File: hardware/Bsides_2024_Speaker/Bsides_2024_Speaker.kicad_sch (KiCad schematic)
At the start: 39 parts, among them J1 Conn_02x03_Odd_Even, J2 Battery, J3 Battery, J4 OLED, P1 USB_C_Plug_USB2.0, Q1 DMG3415U-7, SW1 ON, SW2 RESET, SW3 BOOT, SW4 RESET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

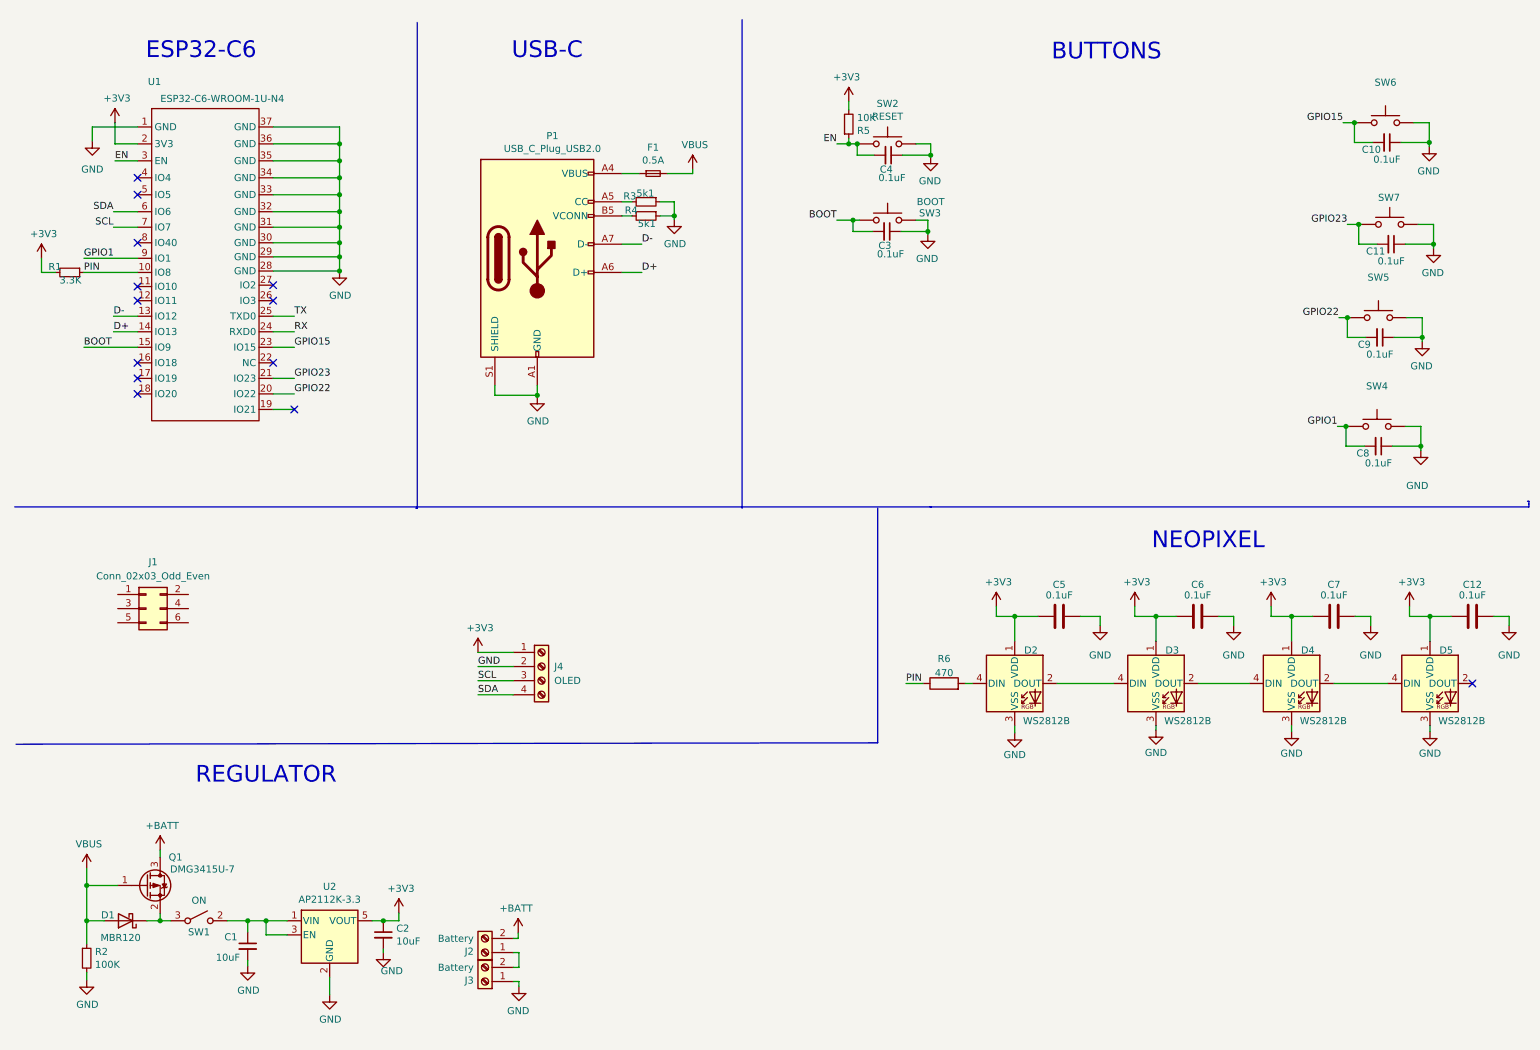
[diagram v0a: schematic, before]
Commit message: feat(Hw):Added_speaker_Badge_Floorplan
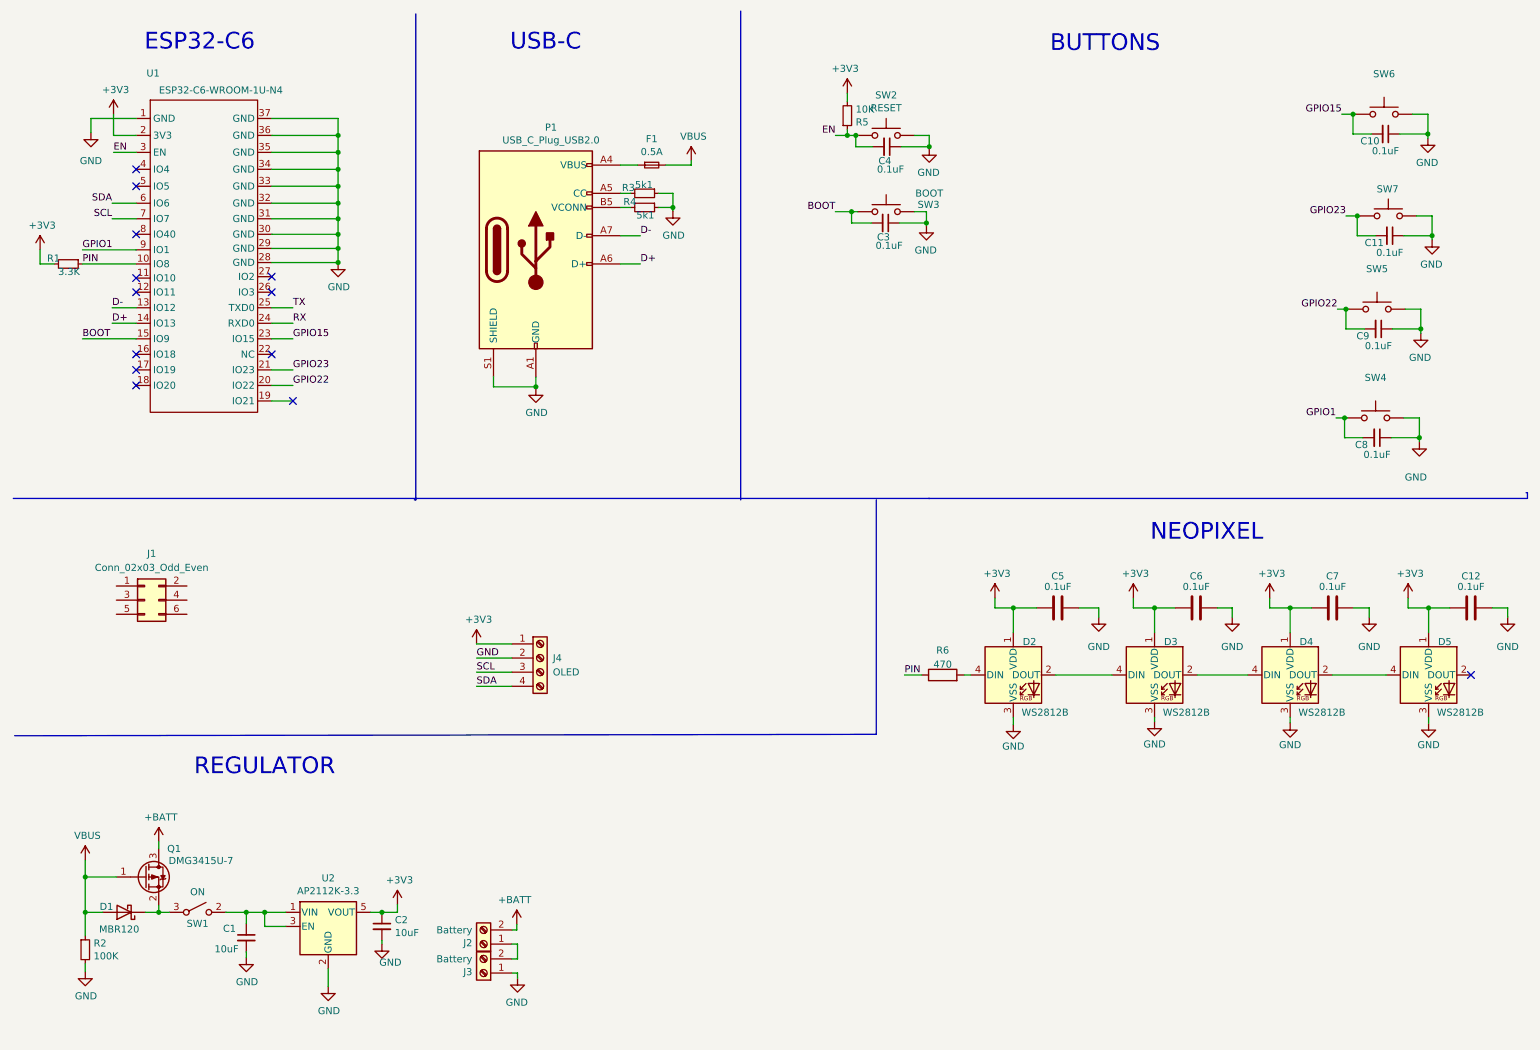
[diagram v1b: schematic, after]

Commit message: feat(Hw):Update_Route_Speaker
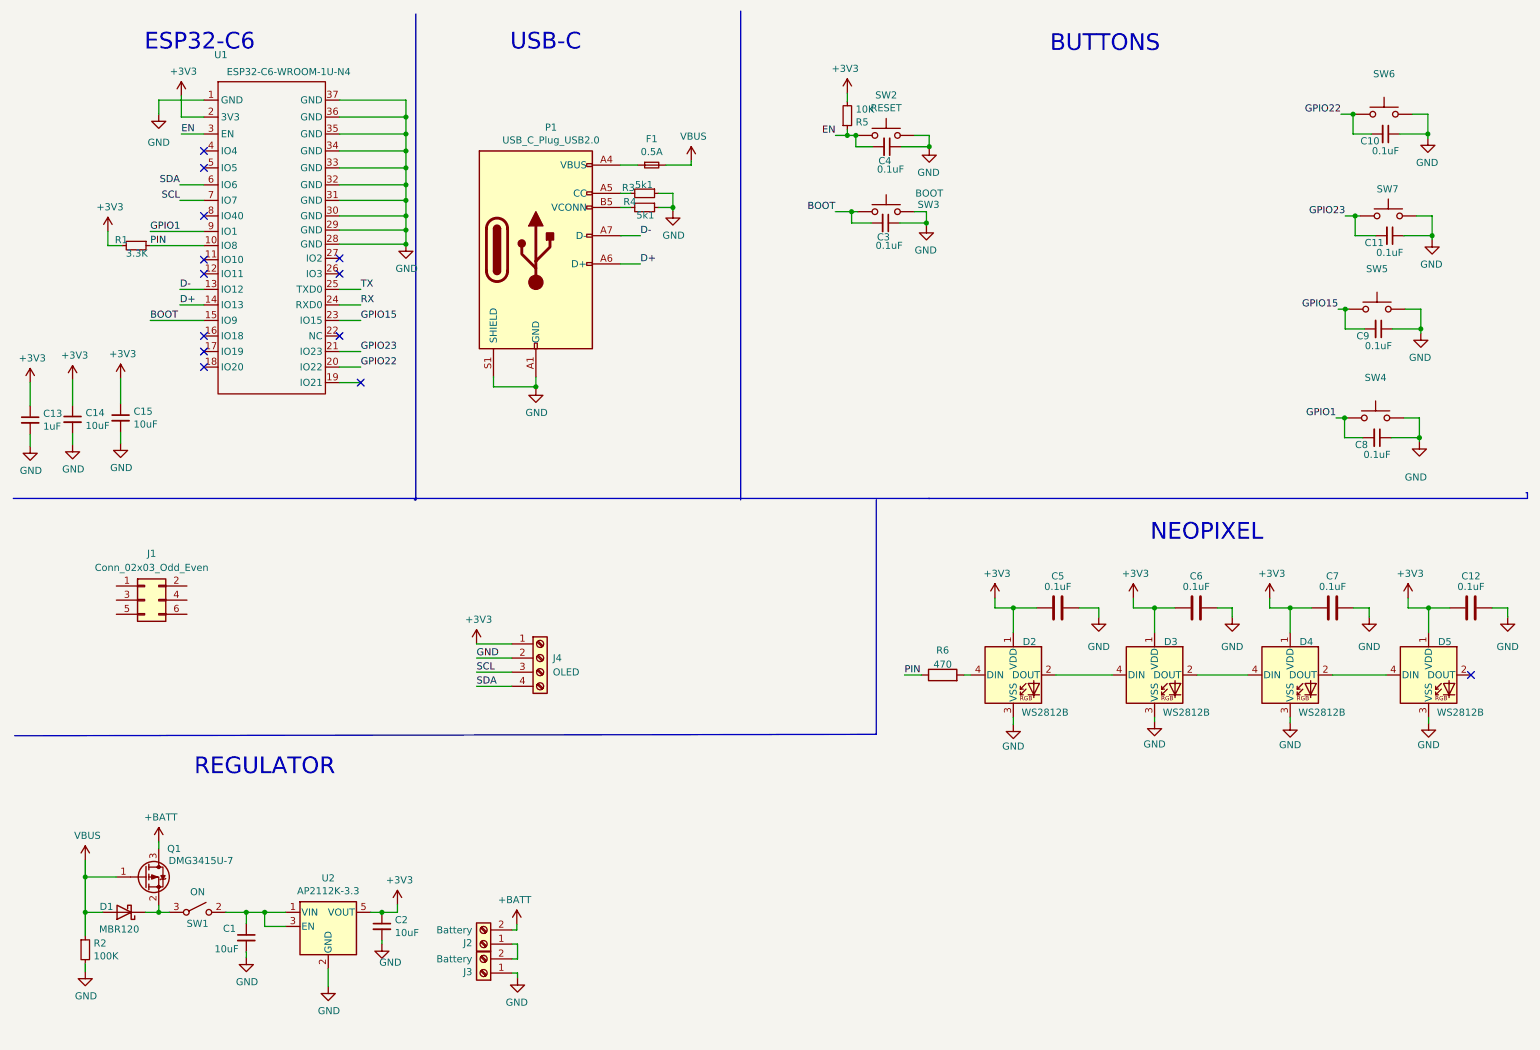
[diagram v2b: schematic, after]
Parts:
- added C13: 1uF, Capacitor_SMD:C_0603_1608Metric, symbol Device:C_Small
- added C14, C15: 10uF, Capacitor_SMD:C_0603_1608Metric, symbol Device:C_Small
- J2, J3: footprint bsides:BH-AAA-A1aj001 -> bsides:BH-AA-A1AJ020
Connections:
- net +3V3: now also C13.1, C14.1, C15.1
- net GND: now also C13.2, C14.2, C15.2
- net GPIO15: now also C9.2, SW5.2; no longer C10.2, SW6.2
- net GPIO22: now also C10.2, SW6.2; no longer C9.2, SW5.2
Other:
- moved on the sheet: R1, U1

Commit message: feat(Hw):Update_PCB_Speaker
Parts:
- J1: value Conn_02x03_Odd_Even -> Add_On
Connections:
- net +3V3: now also J1.1 (Pin_1)
- net GND: now also J1.2 (Pin_2)
- net GPIO1: now also U1.26 (IO3); no longer U1.9 (IO1)
- net SCL: now also J1.4 (Pin_4)
- net SDA: now also J1.3 (Pin_3)
- no-connect marks 13 -> 14
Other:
- moved on the sheet: J2, J3

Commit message: feat:(Hw)Update_PCB_Speaker_Sponsor_Staff
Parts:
- C1, C14, C15, C2: Proveedor (none) -> Mouser; manf# (none) -> GRM188R61E106KA73J
- C10, C11, C8, C9: LCSC# (none) -> C478888; Proveedor (none) -> Mouser; manf# (none) -> KAM15AR71C104KM
- C12, C5, C6, C7: LCSC# C42998 -> C478888; Proveedor LCSC -> Mouser; manf# 0603F104M500NT -> KAM15AR71C104KM
- C13: Proveedor (none) -> Mouser; manf# (none) -> TMK107BJ105KA8T
- C3, C4: Proveedor (none) -> Mouser; manf# (none) -> KAM15AR71C104KM
- D1: Proveedor (none) -> Mouser; manf# MBR120LSF -> MBR120LSFT1G
- D2, D3, D4, D5: manf# WS2812B-Mini -> (none)
- F1: LCSC# - -> (none); Proveedor (none) -> Mouser; manf# MFU0805FF00500P100 -> MFU0805FF00750P100
- P1: Proveedor (none) -> Mouser; manf# TYPE-C-31-M-31 -> USB4105-GF-A
- Q1: Proveedor (none) -> Mouser; manf# DMG3415U-7 -> DMG3415UQ-7
- R1: Proveedor (none) -> Mouser; manf# (none) -> ERJ-3GEYJ332V
- R2: Proveedor LCSC -> Mouser; manf# (none) -> RC0603DR-07100KL
- R3, R4: Proveedor (none) -> Mouser; manf# ERJ3RBD5101V -> AC0603DR-075K1L
- R5: Proveedor (none) -> Mouser; manf# CR-03JL7---10K -> RMC1/16K1002DTP
- R6: Proveedor (none) -> Mouser; manf# RTT03471JTP -> ERJ-3RBD4700V
- SW1, U2: Proveedor (none) -> Mouser
- SW2, SW3, SW5, SW7: Proveedor (none) -> Mouser; manf# (none) -> TL3342F160QG
- SW4, SW6: LCSC# C2886897 -> C318889; Proveedor (none) -> Mouser; manf# (none) -> TL3342F160QG
- U1: value ESP32-C6-WROOM-1U-N4 -> ESP32-C6-WROOM-1-N4; Proveedor (none) -> Mouser; manf# ESP32-C6-WROOM-1U-N4 -> ESP32-C6-WROOM-1-N4
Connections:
- net VBUS: now also C1.1, U2.1 (VIN), U2.3 (EN); no longer D1.2 (A), Q1.1 (G), R2.1
- net +3V3 renamed VOUT
- net VOUT: now also SW1.2 (B); no longer C2.1, U2.5 (VOUT)
- new net: C2.1, D1.2 (A), Q1.1 (G), R2.1, U2.5 (VOUT)
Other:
- moved on the sheet: D1, J2, J3, Q1, R2, SW1

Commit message: First_Route_Speaker
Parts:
- added J5: Serial_IN, Connector_PinHeader_2.54mm:PinHeader_1x03_P2.54mm_Vertical, symbol Connector:Conn_01x03_Socket
- added J6: Serial_OUT, Connector_PinSocket_2.54mm:PinSocket_1x03_P2.54mm_Vertical, symbol Connector:Conn_01x03_Socket
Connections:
- net GND: now also J5.3 (Pin_3), J6.3 (Pin_3)
- net RX: now also J5.2 (Pin_2), J6.1 (Pin_1)
- net TX: now also J5.1 (Pin_1), J6.2 (Pin_2)

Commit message: feat(Hw): Update schematics
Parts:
- J4: manf# I2C SH1106 Display Oled Azul 128×64 1.3 ” -> Display OLED 128×32 0.91 I2C SSD1306 Blanco / Azul
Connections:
- net GND: now also J4.4 (Pin_4); no longer J4.2 (Pin_2)
- net SCL: now also J4.2 (Pin_2); no longer J4.3 (Pin_3)
- net SDA: now also J4.1 (Pin_1); no longer J4.4 (Pin_4)
- net VOUT: now also J4.3 (Pin_3); no longer J4.1 (Pin_1)
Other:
- moved on the sheet: J1, J4, J5, J6, R1, U1

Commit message: feat(Hw):Update_Sch_Speaker
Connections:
- net GPIO1: now also U1.9 (IO1); no longer U1.26 (IO3)
- net PIN: now also U1.11 (IO10); no longer R1.1, U1.10 (IO8)
- net GPIO3: now reaches J1.5 (Pin_5)
- net GPIO3: now also U1.26 (IO3)
- net GPIO2: now reaches J1.6 (Pin_6)
- net GPIO2: now also U1.27 (IO2)
- net GPIO4: now reaches U1.4 (IO4)
- net GPIO4: now also J6.1 (Pin_1)
- net GPIO5: now reaches U1.5 (IO5)
- net GPIO5: now also J6.2 (Pin_2)
- net RX renamed GPIO17
- net GPIO17: no longer J6.1 (Pin_1)
- net TX renamed GPIO16
- net GPIO16: no longer J6.2 (Pin_2)
- new net: R1.1, U1.10 (IO8)
- no-connect marks 14 -> 8

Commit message: feat(Hw):Update_Csv_Speaker
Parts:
- C1, C10, C11, C12, C13, C14, C15, C2, C3, C4, C5, C6, C7, C8, C9, D1, Q1, R2, R5, SW3: Proveedor Mouser -> JLCPCB
- D2, D3, D4, D5: Proveedor LCSC -> JLCPCB
- F1: value 0.5A -> 0.75A; LCSC# (none) -> C1972808; Proveedor Mouser -> JLCPCB
- J1: LCSC# (none) -> C5116527; Proveedor (none) -> JLCPCB
- J2, J3: Proveedor (none) -> JLCPCB; manf# - -> (none)
- J4: Proveedor (none) -> UNIT ELECTRONICS
- J5: LCSC# (none) -> C5333416; Proveedor (none) -> JLCPCB
- J6: LCSC# (none) -> C5116529; Proveedor (none) -> JLCPCB
- P1: LCSC# C2987386 -> C393939; Proveedor Mouser -> JLCPCB
- R1: LCSC# (none) -> C403480; Proveedor Mouser -> JLCPCB
- R3, R4: LCSC# C191782 -> C113390; Proveedor Mouser -> JLCPCB
- SW1: LCSC# - -> C431540; Proveedor Mouser -> JLCPCB; manf# JS102011SAQN -> (none)
- SW2, SW4, SW6: value RESET -> SW; Proveedor Mouser -> JLCPCB
- SW5, SW7: value ~ -> SW; LCSC# C2886897 -> C318889; Proveedor Mouser -> JLCPCB
- U2: LCSC# C150742 -> C3021085; manf# AP7365-33WG-7 -> AP2112K3.3TRG
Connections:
- net GPIO1 renamed LEFT
- net GPIO15 renamed RIGHT
- net GPIO16 renamed TX
- net GPIO17 renamed RX
- net GPIO22 renamed UP
- net GPIO23 renamed DOWN
- net GPIO4 renamed RX1
- net GPIO5 renamed TX1
